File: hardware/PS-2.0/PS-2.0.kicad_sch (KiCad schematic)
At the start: 51 parts, among them J1 PinSocket_02x16_P2.54mm_Verti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, J2 Conn_01x05, J3 Conn_01x05, J8 Conn_01x03, J9 Conn_01x03, K1 RAYEX-L90, K2 RAYEX-L90, Q1 IRFPE50, Q2 IRFPE50, Q3 IRFPE50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

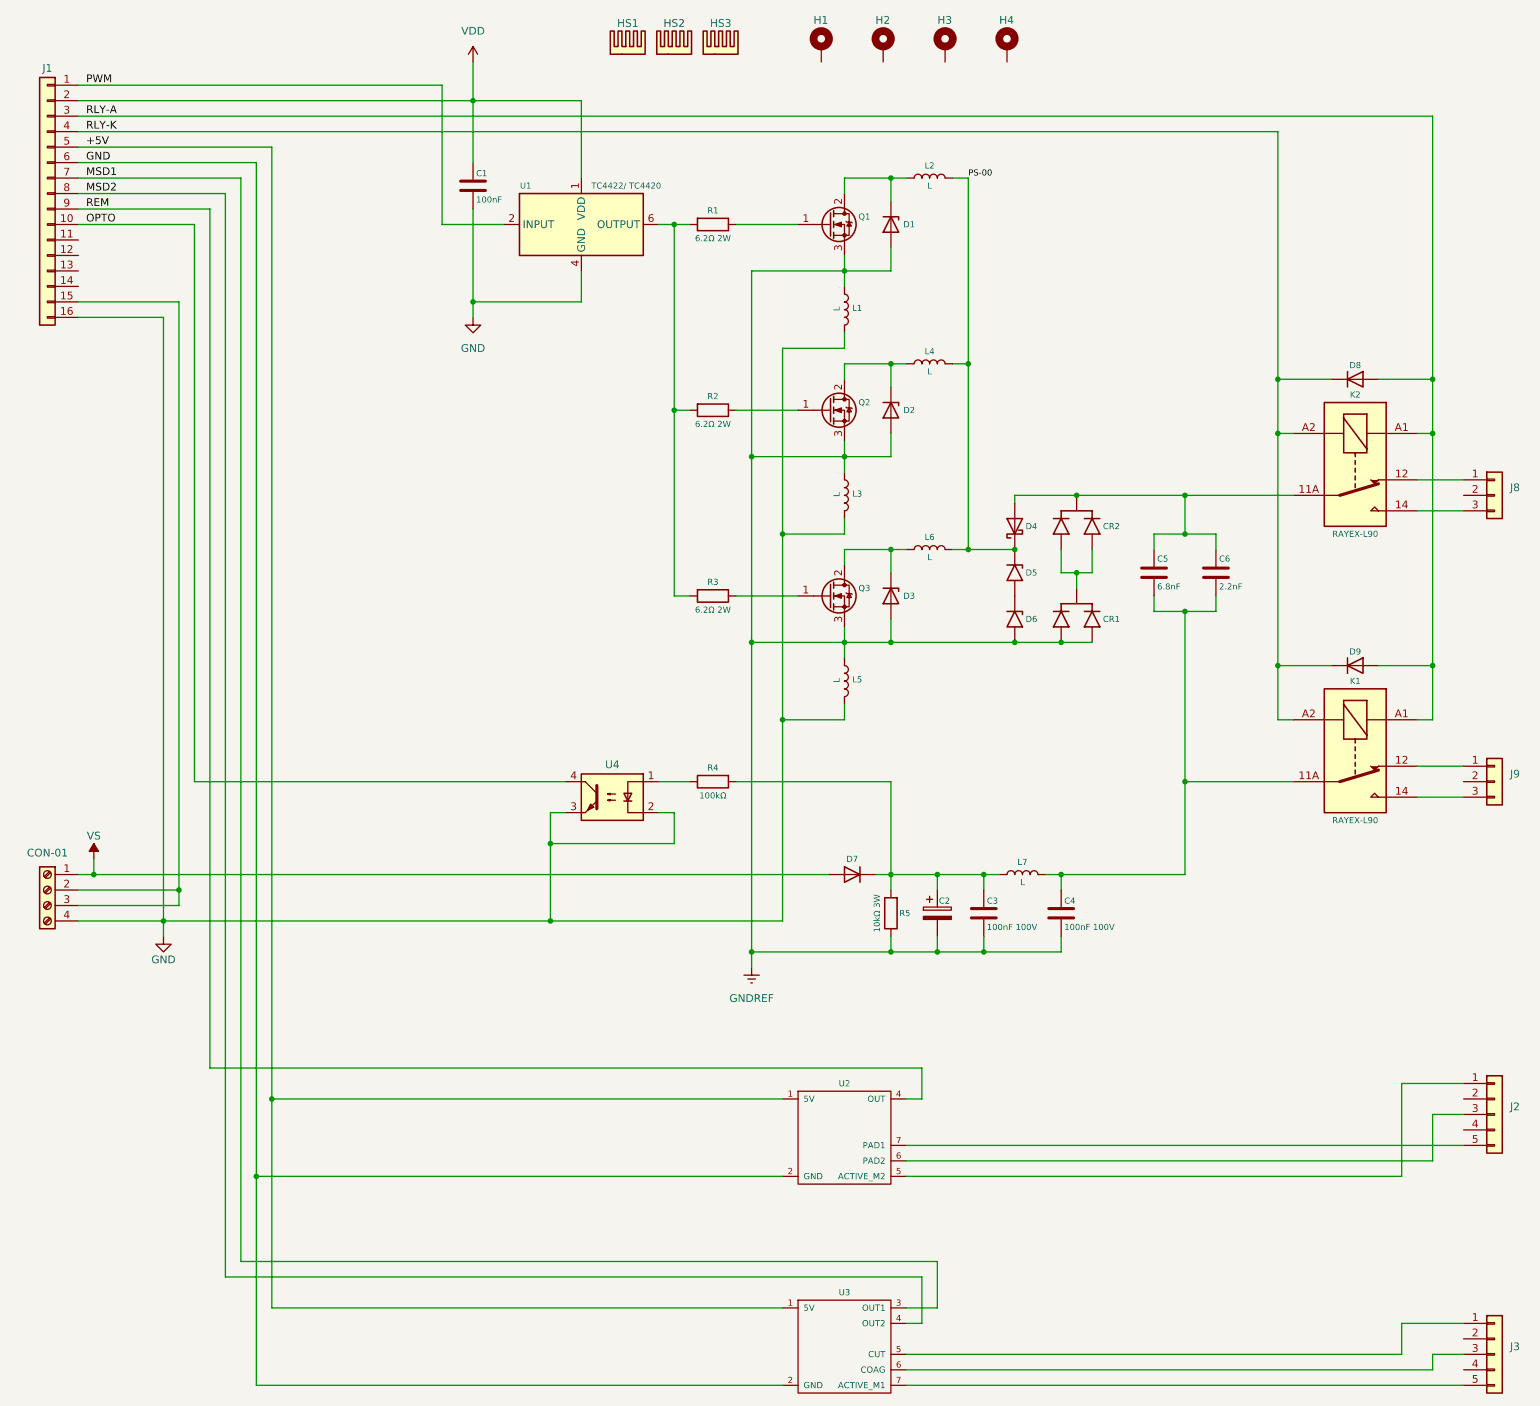
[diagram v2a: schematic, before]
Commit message: modified:   README.md 	deleted:    hardware/CTL-1.0/CTL-1.0-backups/CTL-1.0-2025-05-27_175205.zip 	deleted:    hardware/CTL-1.0/CTL-1.0-backups/CTL-1.0-2025-05-27_180035.zip 	deleted:    hardware/CTL-1.0/CTL-1.0-backups/CTL-1.0-2025-05-27_181441.zip 	deleted:    hardware/CTL-1.0/CTL-1.0-backups/CTL-1.0-2025-05-27_182529.zip 	deleted:    hardware/CTL-1.0/CTL-1.0-backups/CTL-1.0-2025-05-27_183819.zip 	deleted:    hardware/CTL-1.0/CTL-1.0-backups/CTL-1.0-2025-05-28_201558.zip 	deleted:    hardware/CTL-1.0/CTL-1.0-backups/CTL-1.0-2025-06-04_091843.zip 	new file:   hardware/CTL-1.0/CTL-1.0-backups/CTL-1.0-2025-06-05_141632.zip 	new file:   hardware/CTL-1.0/CTL-1.0-backups/CTL-1.0-2025-06-05_142549.zip 	new file:   hardware/CTL-1.0/CTL-1.0-backups/CTL-1.0-2025-06-05_143053.zip 	new file:   hardware/CTL-1.0/CTL-1.0-backups/CTL-1.0-2025-06-05_144242.zip 	new file:   hardware/CTL-1.0/CTL-1.0-backups/CTL-1.0-2025-06-05_144757.zip 	new file:   hardware/CTL-1.0/CTL-1.0-backups/CTL-1.0-2025-06-05_145506.zip 	modified:   hardware/CTL-1.0/CTL-1.0.kicad_pcb 	modified:   hardware/CTL-1.0/CTL-1.0.kicad_prl 	modified:   hardware/CTL-1.0/CTL-1.0.kicad_sch 	modified:   hardware/CTL-1.0/fp-info-cache 	new file:   hardware/PS-2.0/PS-2.0-backups/PS-2.0-2025-06-05_110653.zip 	new file:   hardware/PS-2.0/PS-2.0-backups/PS-2.0-2025-06-05_111332.zip 	new file:   hardware/PS-2.0/PS-2.0-backups/PS-2.0-2025-06-05_115228.zip 	new file:   hardware/PS-2.0/PS-2.0-backups/PS-2.0-2025-06-05_125334.zip 	modified:   hardware/PS-2.0/PS-2.0.kicad_pcb 	modified:   hardware/PS-2.0/PS-2.0.kicad_prl 	modified:   hardware/PS-2.0/PS-2.0.kicad_sch 	deleted:    hardware/PS-2.0/~PS-2.0.kicad_pcb.lck 	deleted:    hardware/PS-2.0/~PS-2.0.kicad_sch.lck 	modified:   pic/.DS_Store
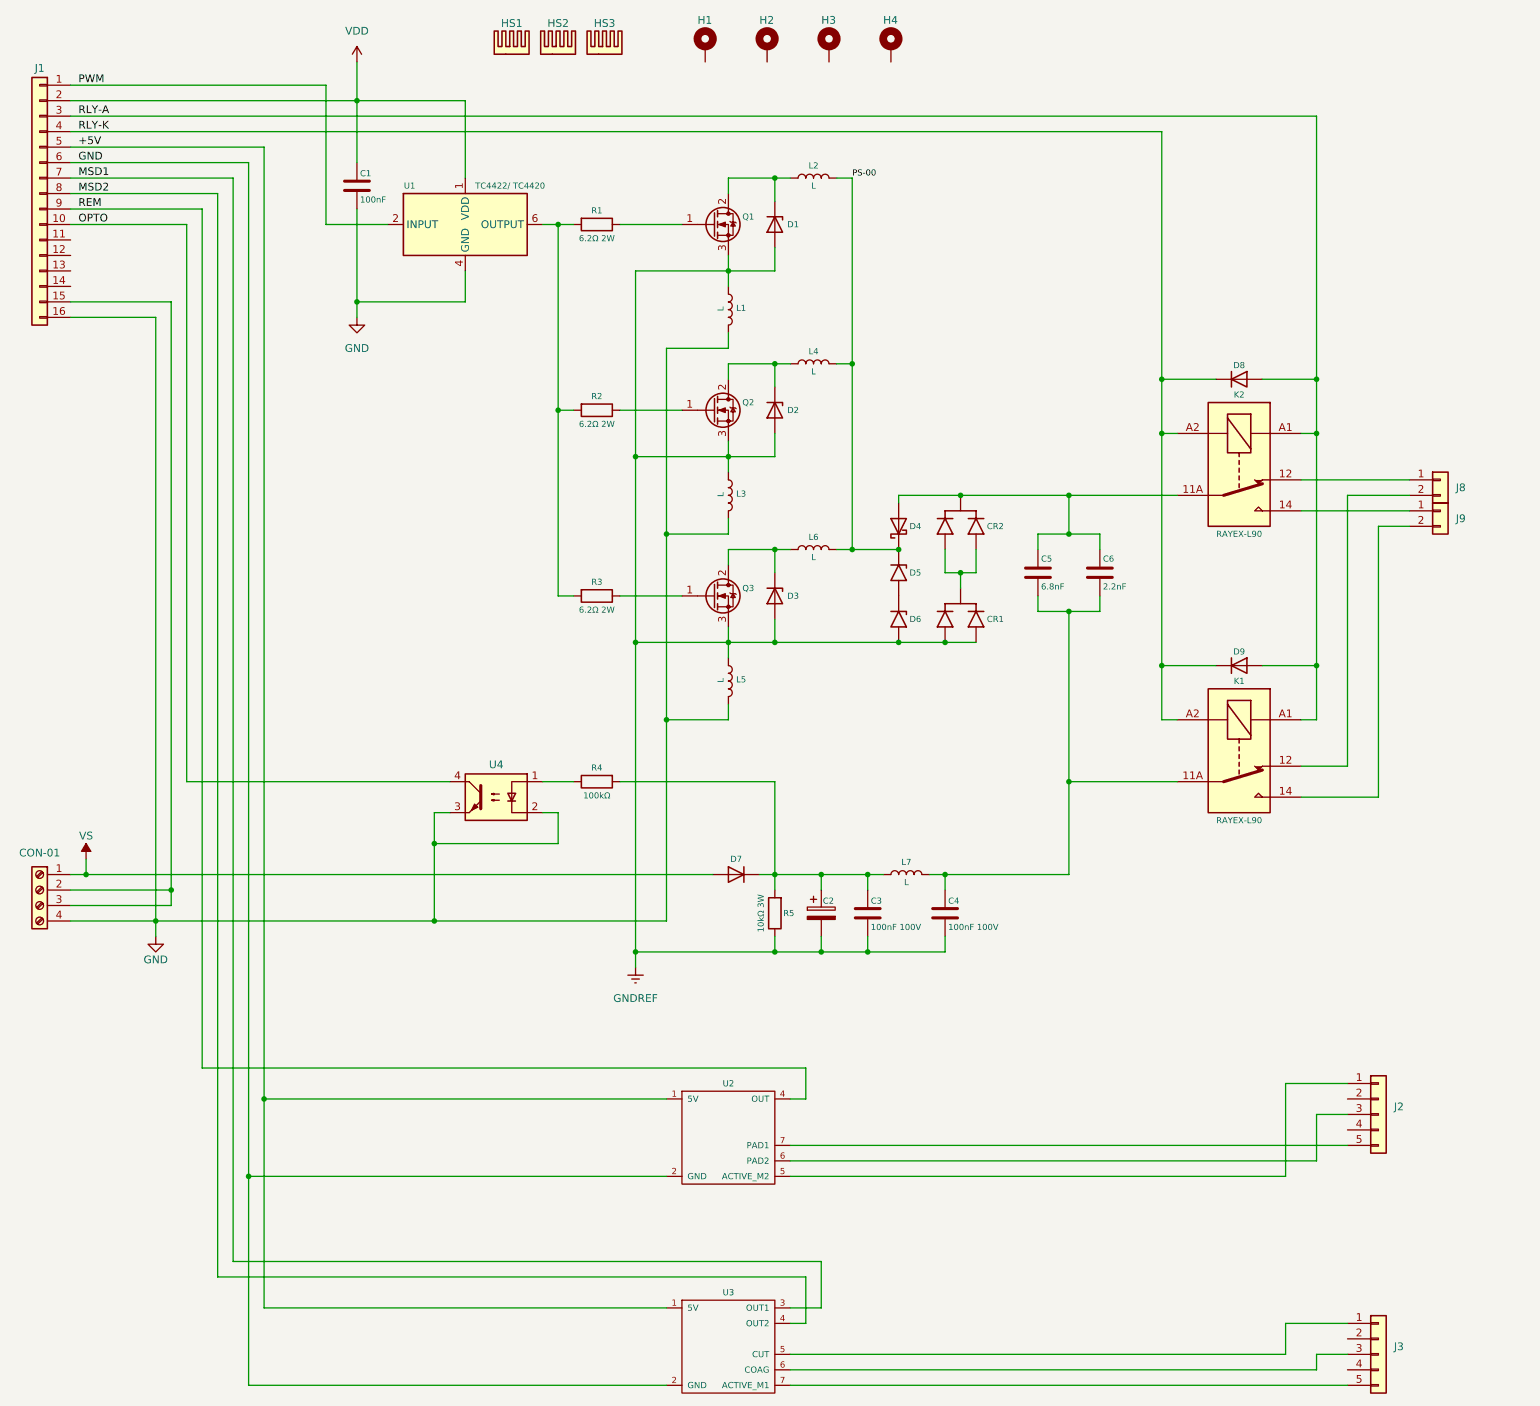
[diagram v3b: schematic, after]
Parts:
- removed J8, J9: Conn_01x03, Connector_Molex:Molex_KK-396_5273-03A_1x03_P3.96mm_Vertical_2, symbol Connector_Generic:Conn_01x03
- added J8, J9: Conn_01x02, Connector_Molex:Molex_KK-396_5273-03A_1x03_P3.96mm_Vertical_2, symbol Connector_Generic:Conn_01x02
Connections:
- net at K2.12: now also J8.1 (Pin_1)
- net at K2.14: now also J9.1 (Pin_1)
- net at K1.12: now also J8.2 (Pin_2)
- net at K1.14: now also J9.2 (Pin_2)
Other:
- moved on the sheet: C1, C2, C3, C4, C5, C6, CON-01, CR1, CR2, D1, D2, D3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

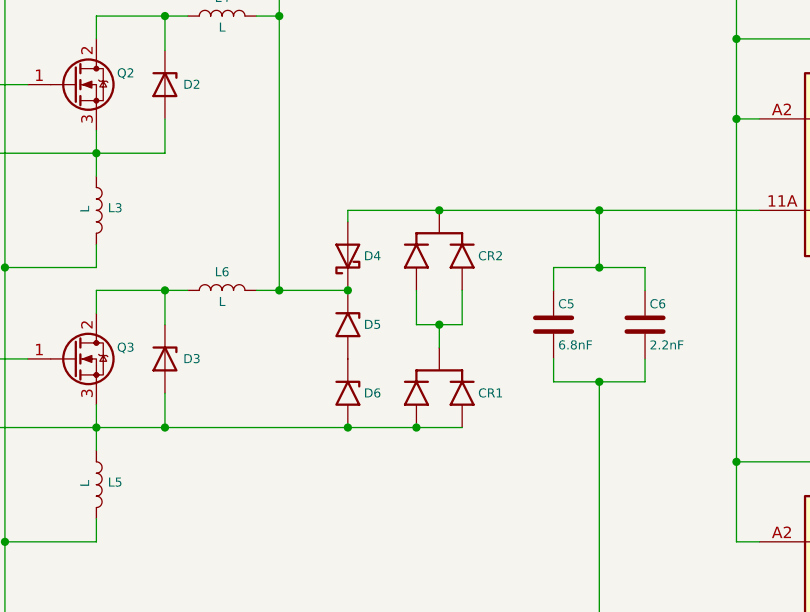
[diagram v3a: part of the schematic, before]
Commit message: modified:   firmware/ESP32-S3 PWM/src/main.cpp new file:   hardware/PS-2.0/PS-2.0-backups/PS-2.0-2025-06-14_145930.zip modified:   hardware/PS-2.0/PS-2.0.kicad_sch modified:   log.md
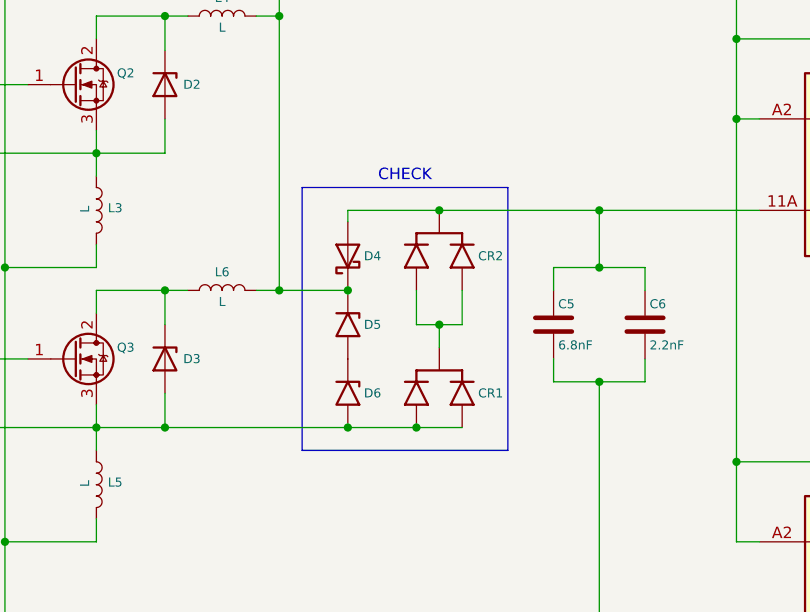
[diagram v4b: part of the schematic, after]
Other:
- note added: "CHECK"
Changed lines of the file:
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@@
+		)
+	)
+	(rectangle
+		(start 163.83 113.03)
+		(end 186.69 142.24)
+		(stroke
+			(width 0)
+			(type default)
+		)
+		(fill
+			(type none)
+		)
+	)
+	(text "CHECK"
+		(exclude_from_sim no)
+		(at 175.26 111.76 0)
+		(effects
+			(font
+				(size 1.27 1.27)
+			)
 		)
 	)

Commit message: modified:   .DS_Store 	new file:   .~Ferrite Transformer Calculation.xlsx 	new file:   .~Voltage.xlsx 	new file:   Ferrite Transformer Calculation.xlsx 	modified:   README.md 	new file:   Voltage.xlsx 	modified:   firmware/ESP32-S3 PWM/src/main.cpp 	deleted:    hardware/CTL-1.0/CTL-1.0-backups/CTL-1.0-2025-05-28_202523.zip 	new file:   hardware/CTL-1.0/CTL-1.0-backups/CTL-1.0-2025-07-03_115731.zip 	new file:   hardware/PS-2.0/PS-2.0-backups/PS-2.0-2025-06-18_154635.zip 	new file:   hardware/PS-2.0/PS-2.0-backups/PS-2.0-2025-06-19_101754.zip 	modified:   hardware/PS-2.0/PS-2.0.kicad_pcb 	modified:   hardware/PS-2.0/PS-2.0.kicad_sch 	new file:   hardware/XF-1.0/XF-1.0-backups/XF-1.0-2025-06-19_140209.zip 	new file:   hardware/XF-1.0/XF-1.0-backups/XF-1.0-2025-06-19_140721.zip 	new file:   hardware/XF-1.0/XF-1.0-backups/XF-1.0-2025-06-19_141456.zip 	new file:   hardware/XF-1.0/XF-1.0-backups/XF-1.0-2025-06-19_142018.zip 	new file:   hardware/XF-1.0/XF-1.0-backups/XF-1.0-2025-06-19_142518.zip 	new file:   hardware/XF-1.0/XF-1.0-backups/XF-1.0-2025-06-28_090149.zip 	new file:   hardware/XF-1.0/XF-1.0-backups/XF-1.0-2025-07-03_112321.zip 	new file:   hardware/XF-1.0/XF-1.0-backups/XF-1.0-2025-07-14_112815.zip 	new file:   hardware/XF-1.0/XF-1.0.kicad_pcb 	new file:   hardware/XF-1.0/XF-1.0.kicad_prl 	new file:   hardware/XF-1.0/XF-1.0.kicad_pro 	new file:   hardware/XF-1.0/XF-1.0.kicad_sch 	new file:   hardware/XF-1.0/fp-info-cache 	renamed:    hardware/PS-2.0/~PS-2.0.kicad_sch.lck -> hardware/XF-1.0/~XF-1.0.kicad_pcb.lck 	new file:   hardware/XF-1.0/~XF-1.0.kicad_sch.lck 	modified:   log.md
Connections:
- net at L4.1, Q2.2 (D): no longer D2.1 (K)
- net at L6.1, Q3.2 (D): no longer D3.1 (K)
- net at Q1.1 (G), R1.1: now also D1.1 (K)
- net at L2.1, Q1.2 (D): no longer D1.1 (K)
- net at Q2.1 (G), R2.1: now also D2.1 (K)
- net at Q3.1 (G), R3.1: now also D3.1 (K)
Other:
- note removed: "CHECK"
- moved on the sheet: D1, D2, D3

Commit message: modified:   README.md 	deleted:    hardware/CTL-1.0/CTL-1.0-backups/CTL-1.0-2025-05-28_203806.zip 	deleted:    hardware/CTL-1.0/CTL-1.0-backups/CTL-1.0-2025-05-28_204313.zip 	deleted:    hardware/CTL-1.0/CTL-1.0-backups/CTL-1.0-2025-05-30_173028.zip 	deleted:    hardware/CTL-1.0/CTL-1.0-backups/CTL-1.0-2025-05-30_174116.zip 	deleted:    hardware/CTL-1.0/CTL-1.0-backups/CTL-1.0-2025-05-30_175122.zip 	new file:   hardware/CTL-1.0/CTL-1.0-backups/CTL-1.0-2025-07-24_151142.zip 	new file:   hardware/CTL-1.0/CTL-1.0-backups/CTL-1.0-2025-07-24_172002.zip 	new file:   hardware/CTL-1.0/CTL-1.0-backups/CTL-1.0-2025-07-25_175122.zip 	new file:   hardware/CTL-1.0/CTL-1.0-backups/CTL-1.0-2025-07-26_120011.zip 	new file:   hardware/CTL-1.0/CTL-1.0-backups/CTL-1.0-2025-07-26_120808.zip 	modified:   hardware/CTL-1.0/CTL-1.0.kicad_pcb 	modified:   hardware/CTL-1.0/CTL-1.0.kicad_pro 	new file:   hardware/CTL-1.0/CTL-1.0.step 	deleted:    hardware/MSD-1.0/MSD-1.0-backups/MSD-1.0-2025-04-11_111943.zip 	deleted:    hardware/MSD-1.0/MSD-1.0-backups/MSD-1.0-2025-04-11_113401.zip 	new file:   hardware/MSD-1.0/MSD-1.0-backups/MSD-1.0-2025-07-25_163151.zip 	new file:   hardware/MSD-1.0/MSD-1.0-backups/MSD-1.0-2025-07-25_171843.zip 	modified:   hardware/MSD-1.0/MSD-1.0.kicad_pcb 	modified:   hardware/MSD-1.0/MSD-1.0.step 	new file:   hardware/MSD-1.1/MSD-1.1-backups/MSD-1.1-2025-07-24_151252.zip 	new file:   hardware/MSD-1.1/MSD-1.1-backups/MSD-1.1-2025-07-25_152939.zip 	new file:   hardware/MSD-1.1/MSD-1.1-backups/MSD-1.1-2025-07-25_162346.zip 	new file:   hardware/MSD-1.1/MSD-1.1-backups/MSD-1.1-2025-07-25_162917.zip 	modified:   hardware/MSD-1.1/MSD-1.1.kicad_pcb 	modified:   hardware/MSD-1.1/MSD-1.1.step 	modified:   hardware/MSD-1.1/fp-info-cache 	new file:   hardware/MSD-2.0/MSD-2.0-backups/MSD-2.0-2025-07-24_151230.zip 	deleted:    hardware/PS-2.0/PS-2.0-backups/PS-2.0-2025-05-07_010425.zip 	deleted:    hardware/PS-2.0/PS-2.0-backups/PS-2.0-2025-05-09_084820.zip 	deleted:    hardware/P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
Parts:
- added H5, H6: MountingHole_Pad, MountingHole:MountingHole_3.2mm_M3_ISO14580_Pad, symbol Mechanical:MountingHole_Pad
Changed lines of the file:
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@@
+	)
+	(symbol
+		(lib_id "Mechanical:MountingHole_Pad")
+		(at 177.8 41.91 0)
+		(unit 1)
+		(exclude_from_sim yes)
+		(in_bom no)
+		(on_board yes)
+		(dnp no)
+		(property "Reference" "H5"
+			(at 176.53 37.592 0)
+			(effects
+				(font
+					(size 1.27 1.27)
+				)
+				(justify left)
+			)
+		)
+		(property "Value" "MountingHole_Pad"
+			(at 180.34 41.9099 0)
+			(effects
+				(font
+					(size 1.27 1.27)
+				)
+				(justify left)
+				(hide yes)
+			)
+		)
+		(property "Footprint" "MountingHole:MountingHole_3.2mm_M3_ISO14580_Pad"
+			(at 177.8 41.91 0)
+			(effects
+				(font
+					(size 1.27 1.27)
+				)
+				(hide yes)
+			)
+		)
+		(property "Datasheet" "~"
+			(at 177.8 41.91 0)
+			(effects
+				(font
+					(size 1.27 1.27)
+				)
+				(hide yes)
+			)
+		)
+		(property "Description" "Mounting Hole with connection"
+			(at 177.8 41.91 0)
+			(effects
+				(font
+					(size 1.27 1.27)
+				)
+				(hide yes)
+			)
+		)
+		(pin "1"
+		)
+		(instances
+			(project "PS-2.0"
+				(path "/3a4da535-700d-4512-9d93-355e5c375ab5"
+					(reference "H5")
+					(unit 1)
+				)
+			)
+		)
 	)
 	(symbol
@@
 					(unit 1)
 				)
+			)
+		)
+	)
+	(symbol
+		(lib_id "Mechanical:MountingHole_Pad")
+		(at 187.96 41.91 0)
+		(unit 1)
+		(exclude_from_sim yes)
+		(in_bom no)
+		(on_board yes)
+		(dnp no)
+		(property "Reference" "H6"
+			(at 186.69 37.592 0)
+			(effects
+				(font
+					(size 1.27 1.27)
+				)
+				(justify left)
+			)
+		)
+		(property "Value" "MountingHole_Pad"
+			(at 190.5 41.9099 0)
+			(effects
+				(font
+					(size 1.27 1.27)
+				)
+				(justify left)
+				(hide yes)
+			)
+		)
+		(property "Footprint" "MountingHole:MountingHole_3.2mm_M3_ISO14580_Pad"
+			(at 187.96 41.91 0)
+			(effects
+				(font
+					(size 1.27 1.27)
+				)
+				(hide yes)
+			)
+		)
+		(property "Datasheet" "~"
+			(at 187.96 41.91 0)
+			(effects
+				(font
+					(size 1.27 1.27)
+				)
+				(hide yes)
+			)
+		)
+		(property "Description" "Mounting Hole with connection"
+			(at 187.96 41.91 0)
+			(effects
+				(font
+					(size 1.27 1.27)
+				)
+				(hide yes)
+			)
+		)
+		(pin "1"
+		)
+		(instances
+			(project "PS-2.0"
+				(path "/3a4da535-700d-4512-9d93-355e5c375ab5"
+					(reference "H6")
+					(unit 1)
+				)
